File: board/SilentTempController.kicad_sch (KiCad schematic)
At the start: 93 parts, among them J1 Barrel_Jack_Switch, J10 Conn_01x02_Pin, J11 Conn_01x02_Pin, J12 Screw_Terminal_01x02, J13 Screw_Terminal_01x02, J14 Screw_Terminal_01x02, J15 Screw_Terminal_01x02, J2 Screw_Terminal_01x02, J3 Conn_01x02_Pin, J4 Screw_Terminal_01x02, J5 Conn_01x02_Pin, J6 Screw_Terminal_01x02, J7 Conn_01x02_Pin, J8 Screw_Terminal_01x02, J9 Conn_01x02_Pin, Q1 2N3904, Q10 2N3904, Q11 2N3906, Q12 IRLZ44N, Q13 2N3904, Q14 2N3904, Q15 2N3906, Q16 IRLZ44N, Q17 2N3904, Q2 2N3906, Q3 IRLZ44N, Q4 2N3904, Q5 2N3904, Q6 2N3904, Q7 2N3906, Q8 IRLZ44N, Q9 2N3904, SW1 SW_Push, SW2 SW_Push, SW3 SW_Push, SW4 SW_Push, SW5 SW_Push, U1 LM7805_TO220

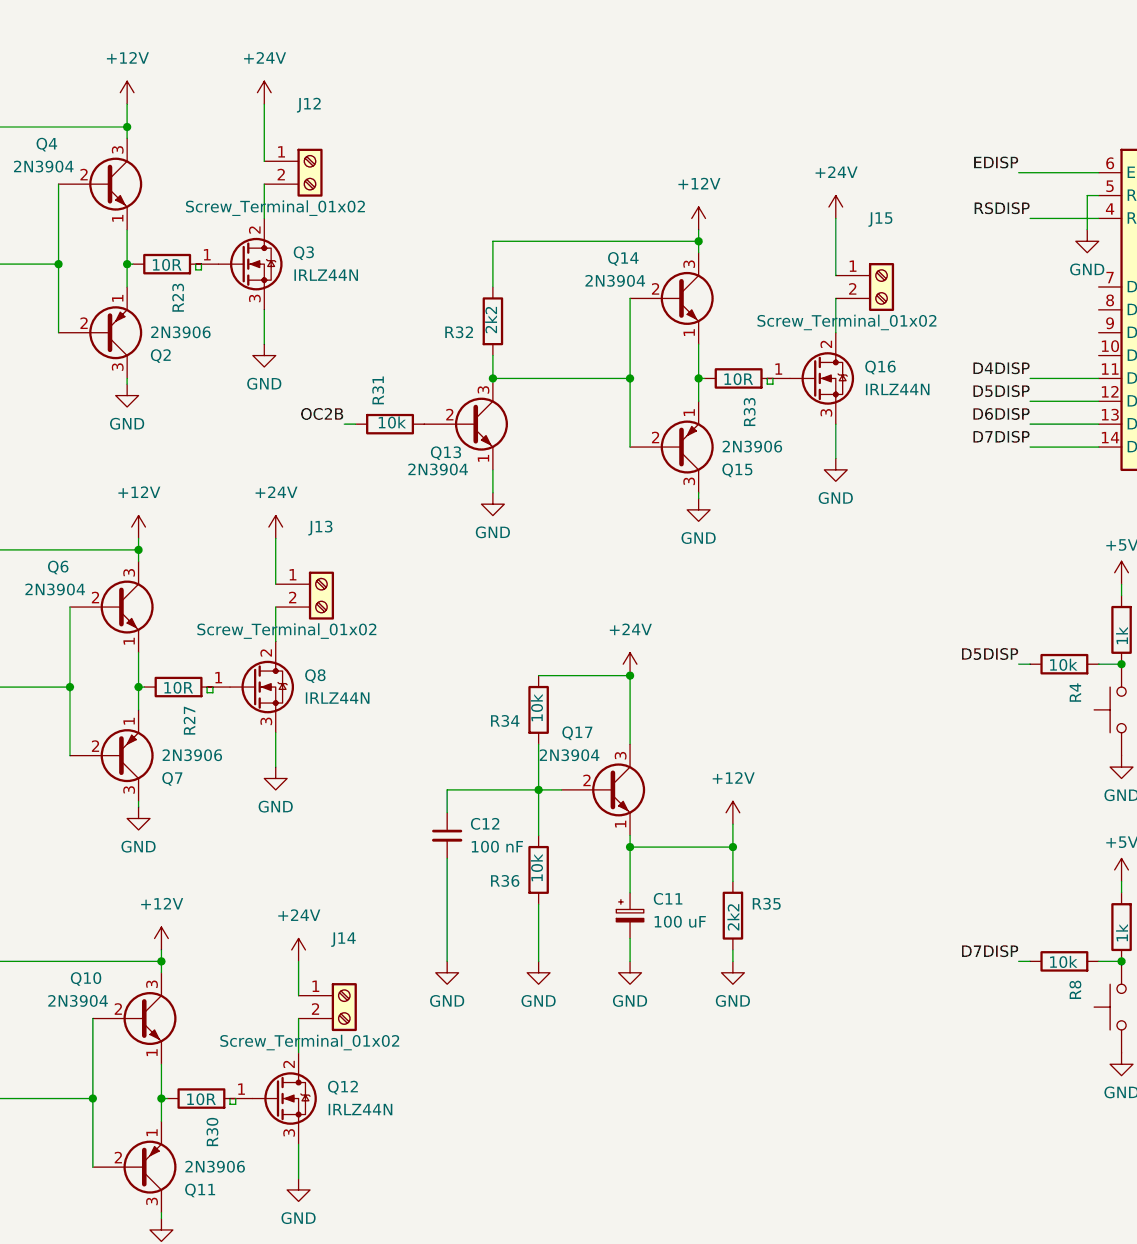
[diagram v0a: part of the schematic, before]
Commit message: Added snubbers
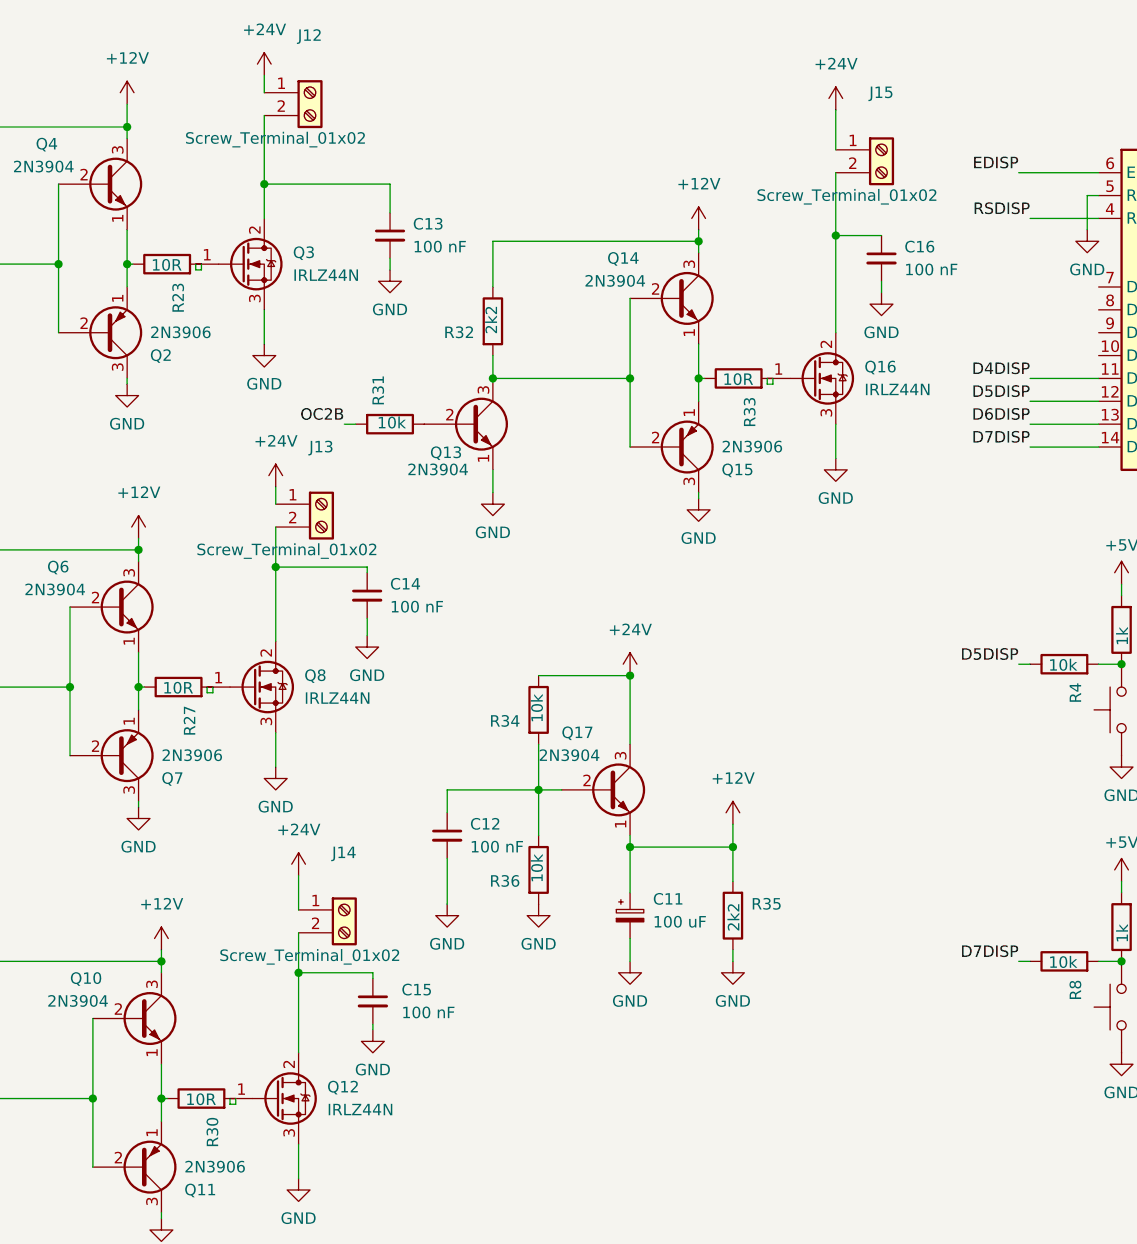
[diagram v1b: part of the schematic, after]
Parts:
- added C13, C14, C15, C16: 100 nF, Capacitor_THT:C_Disc_D5.0mm_W2.5mm_P5.00mm, symbol Device:C_Small
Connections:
- net GND: now also C13.2, C14.2, C15.2, C16.2
- net at J12.2 (Pin_2), Q3.2 (D): now also C13.1
- net at J14.2 (Pin_2), Q12.2 (D): now also C15.1
- net at J13.2 (Pin_2), Q8.2 (D): now also C14.1
- net at J15.2 (Pin_2), Q16.2 (D): now also C16.1
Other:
- moved on the sheet: J12, J13, J14, J15

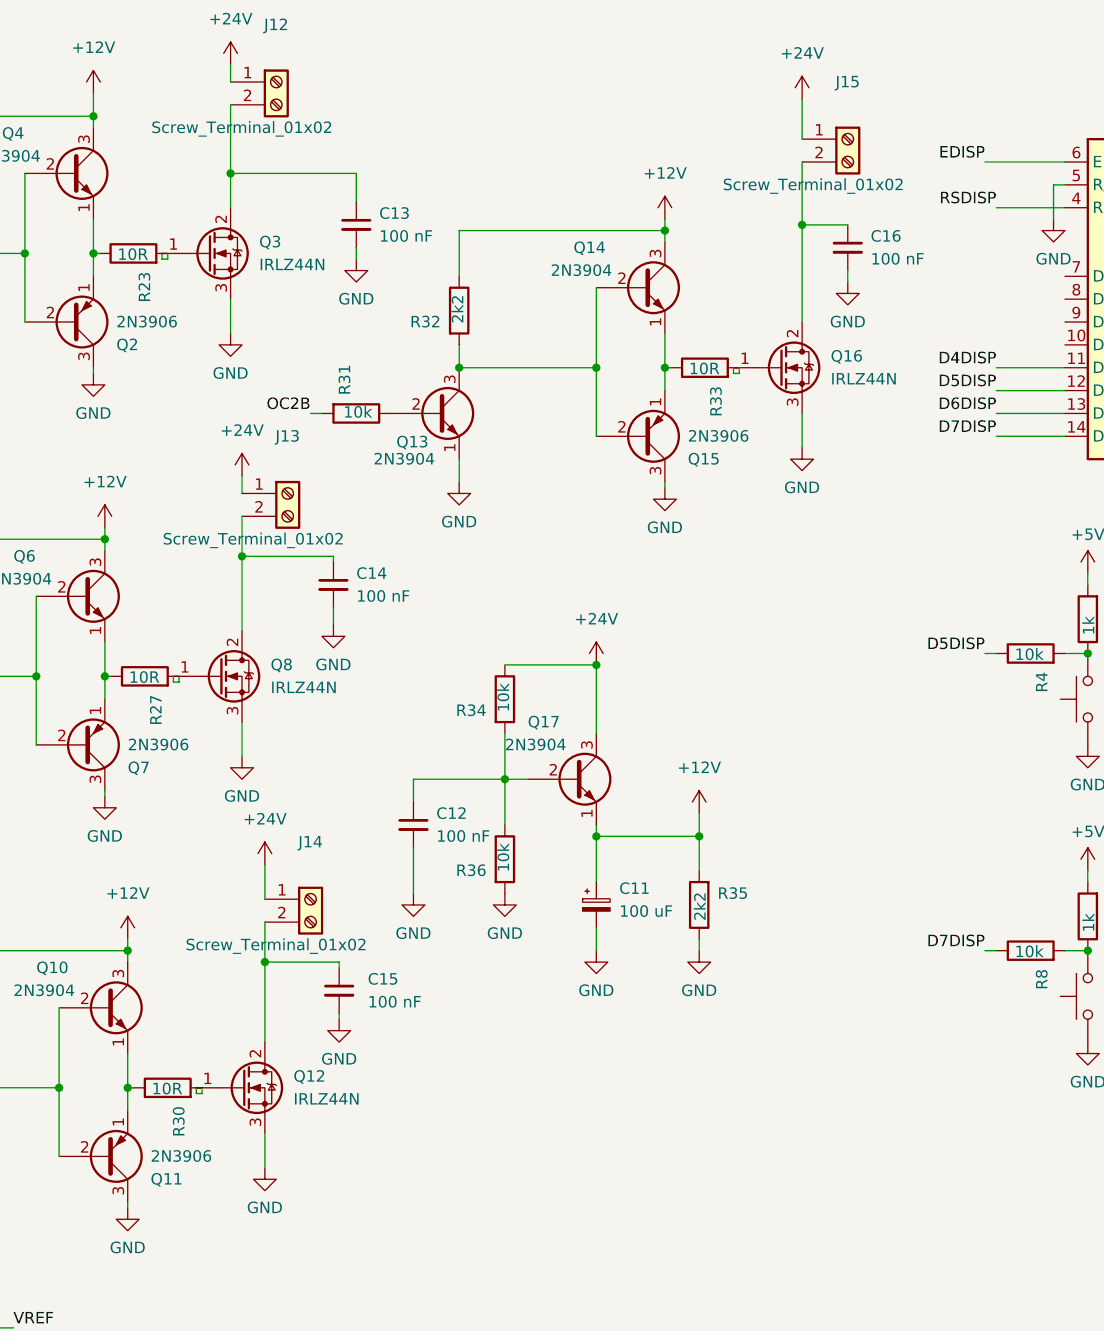
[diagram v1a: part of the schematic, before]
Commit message: improved snubbers
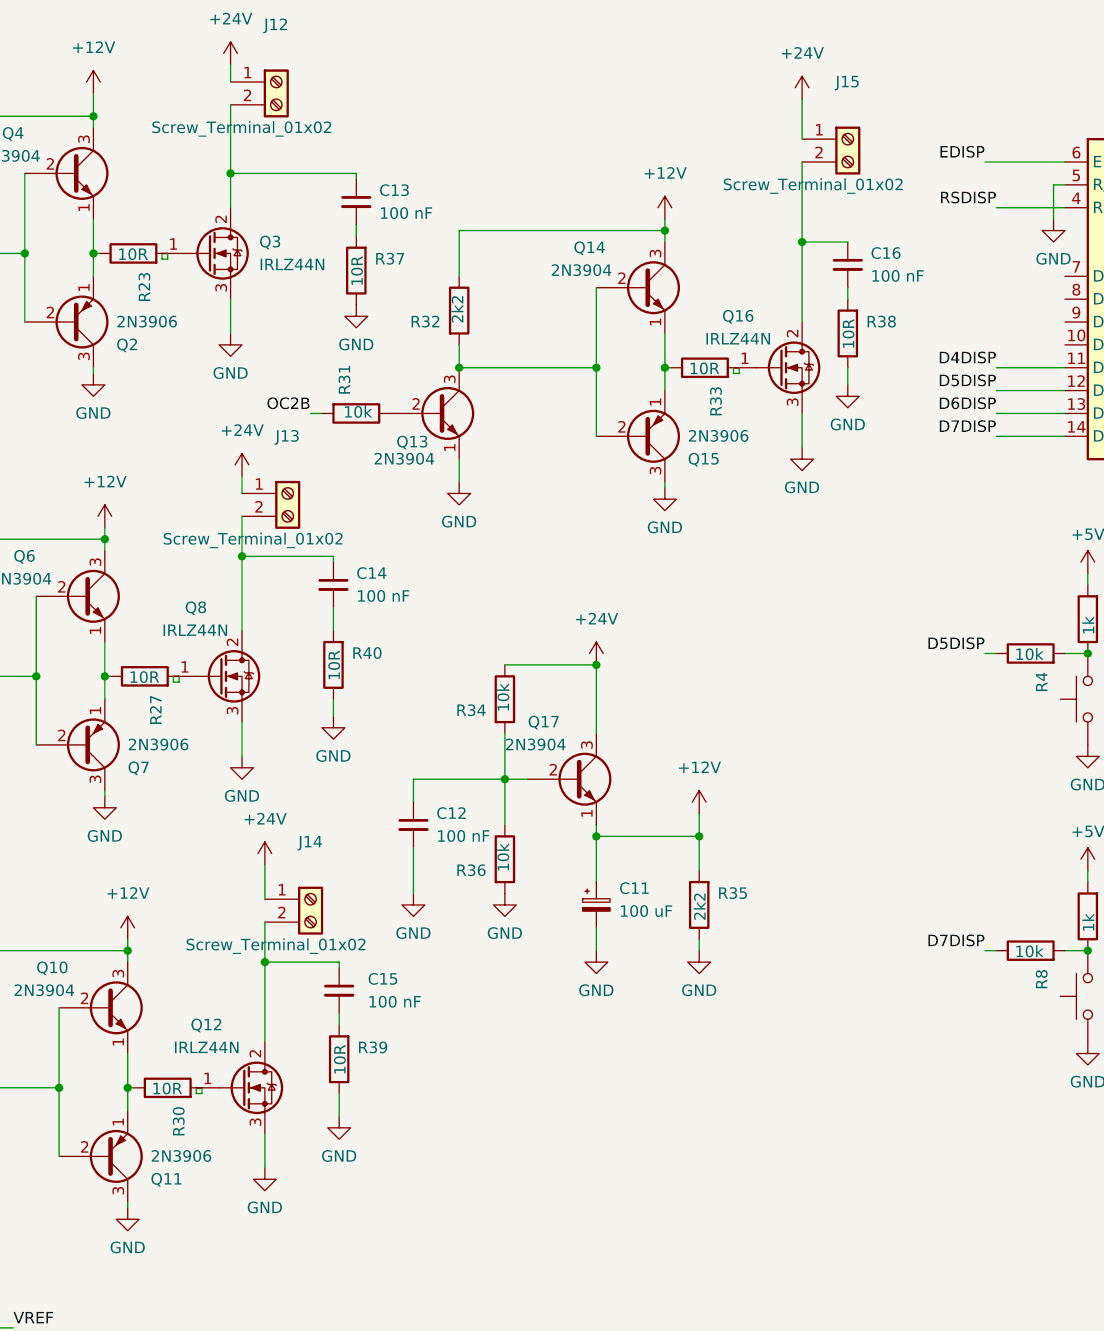
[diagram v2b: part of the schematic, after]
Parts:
- added R37, R38, R39, R40: 10R, Resistor_THT:R_Axial_DIN0207_L6.3mm_D2.5mm_P7.62mm_Horizontal, symbol Device:R
- R33: footprint Resistor_THT:R_Axial_DIN0207_L6.3mm_D2.5mm_P7.62mm_Horizontal -> Resistor_THT:R_Axial_DIN0207_L6.3mm_D2.5mm_P10.16mm_Horizontal
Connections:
- net GND: now also R37.1, R38.1, R39.1, R40.1; no longer C13.2, C14.2, C15.2, C16.2
- new net: C14.2, R40.2
- new net: C13.2, R37.2
- new net: C16.2, R38.2
- new net: C15.2, R39.2
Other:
- moved on the sheet: C13, C16

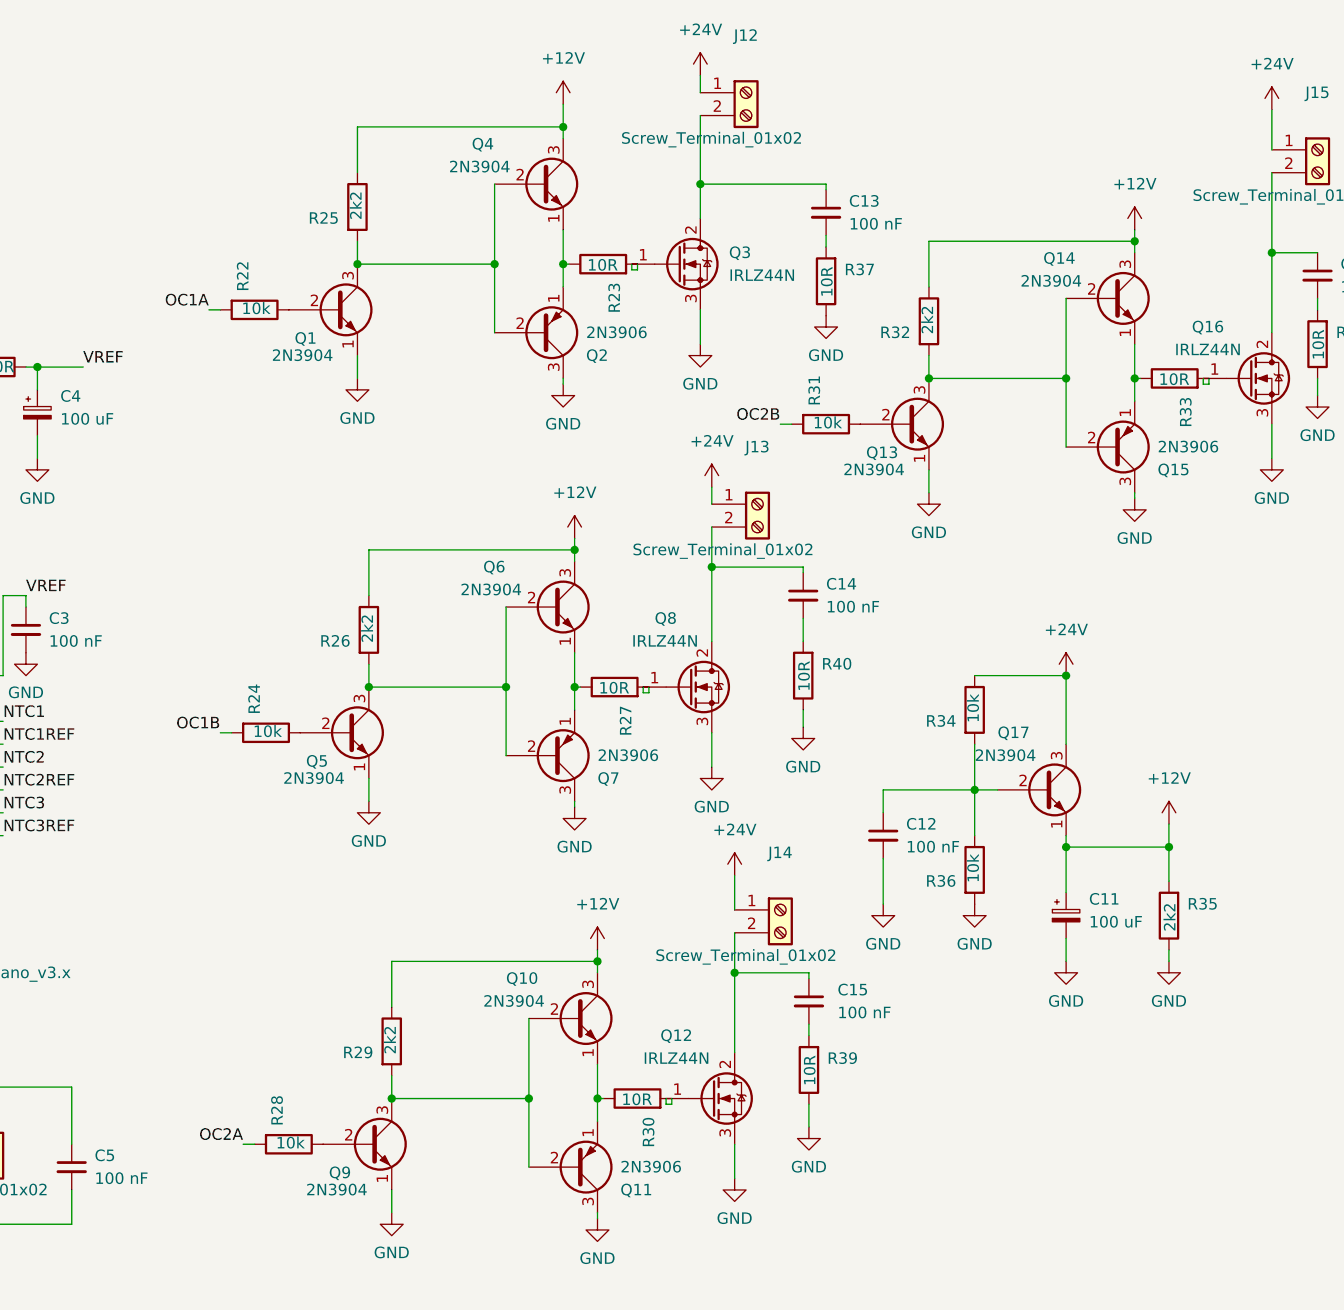
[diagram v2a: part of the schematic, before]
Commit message: Added on protection
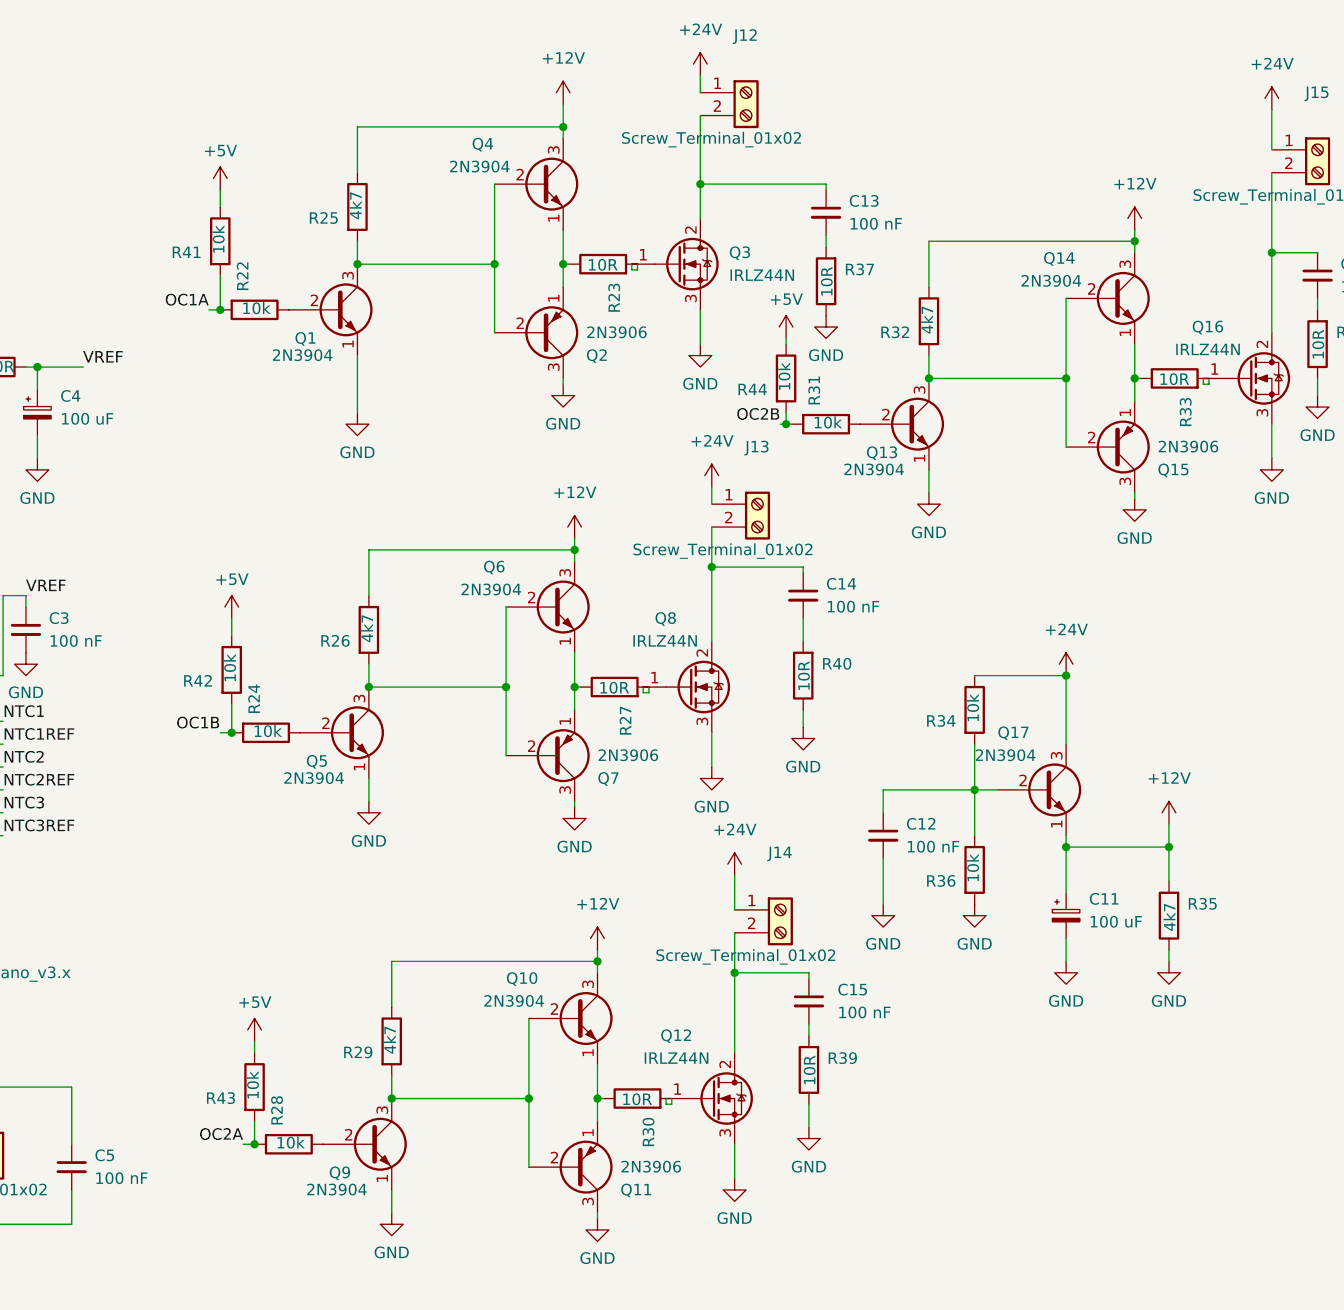
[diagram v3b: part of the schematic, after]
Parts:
- added R41, R42, R43, R44: 10k, Resistor_THT:R_Axial_DIN0207_L6.3mm_D2.5mm_P7.62mm_Horizontal, symbol Device:R
- R25, R26, R29, R32, R35: value 2k2 -> 4k7
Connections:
- net +5V: now also R41.1, R42.1, R43.1, R44.1
- net OC1A: now also R41.2
- net OC1B: now also R42.2
- net OC2A: now also R43.2
- net OC2B: now also R44.2
